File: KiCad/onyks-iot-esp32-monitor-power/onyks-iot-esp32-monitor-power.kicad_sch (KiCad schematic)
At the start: 16 parts, among them J1 Uart_con, J2 Jtag_con, SW1 reset, U1 ESP32-WROOM-32D, U2 ADS1115IDGS

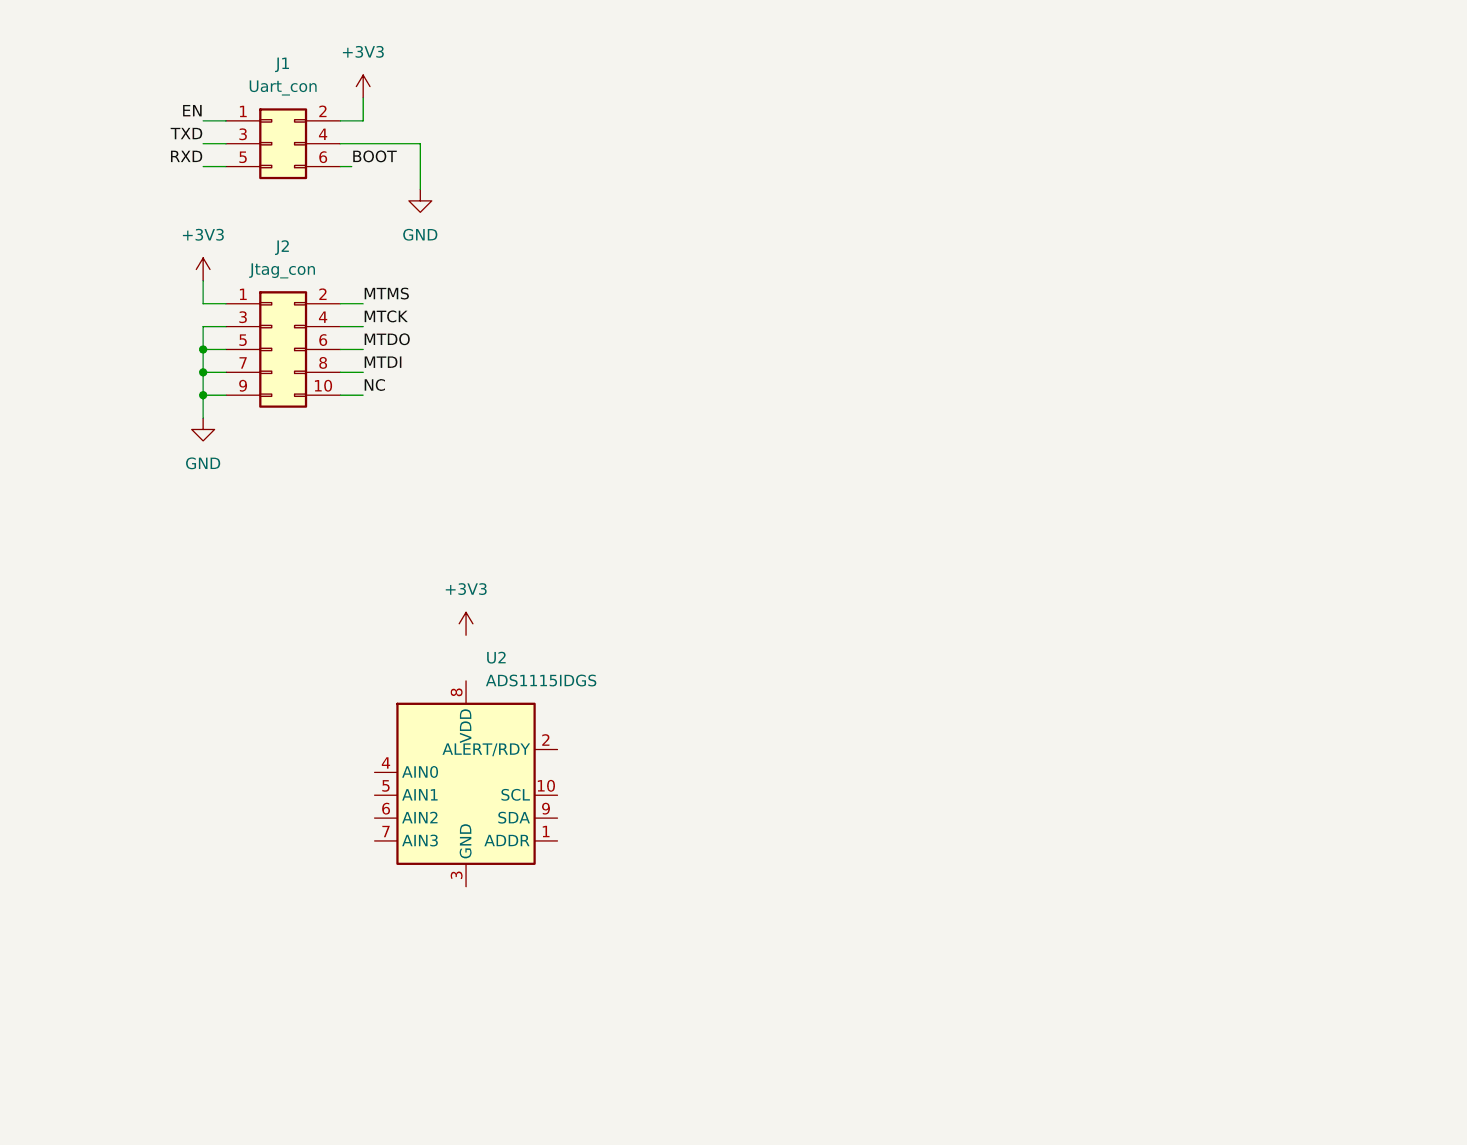
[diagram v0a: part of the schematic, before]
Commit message: Add ACS712 and ADS1115
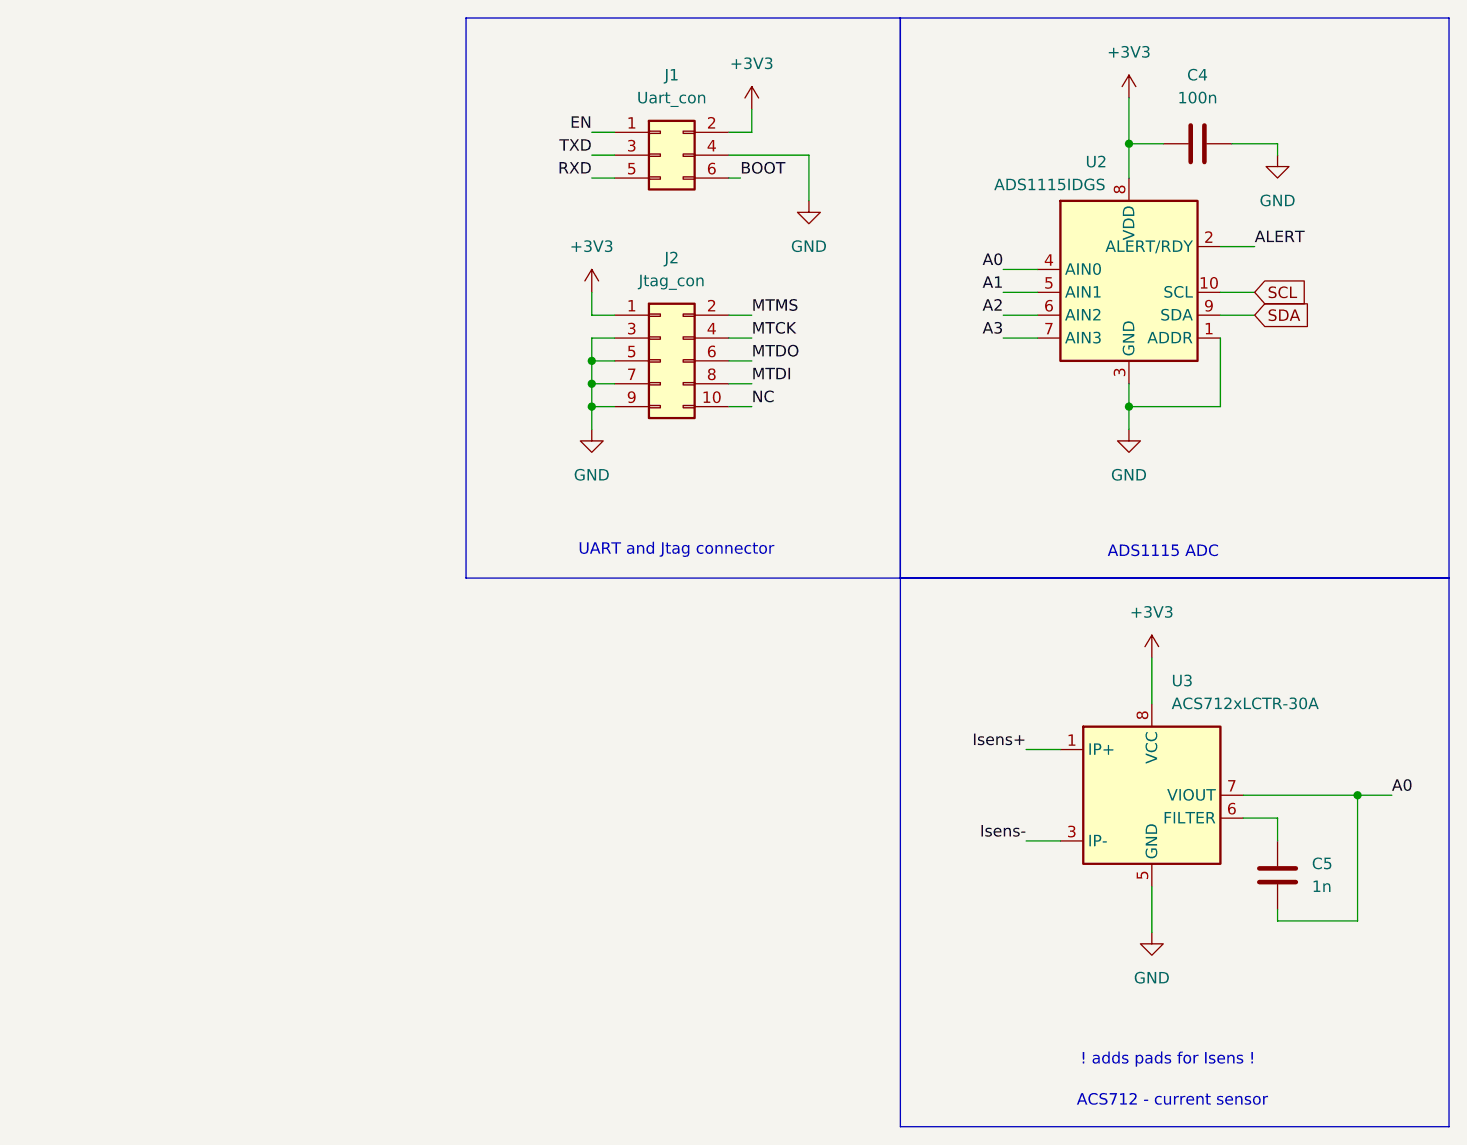
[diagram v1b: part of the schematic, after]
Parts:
- added C4: 100n, Capacitor_SMD:C_0805_2012Metric_Pad1.18x1.45mm_HandSolder, symbol Device:C
- added C5: 1n, symbol Device:C
- added U3: ACS712xLCTR-30A, Package_SO:SOIC-8_3.9x4.9mm_P1.27mm, symbol Sensor_Current:ACS712xLCTR-30A
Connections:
- net +3V3: now also U2.8 (VDD), C4.1, U3.8 (VCC)
- net ALERT: now also U2.2 (ALERT/RDY)
- net GND: now also U2.1 (ADDR), U2.3 (GND), C4.2, U3.5 (GND)
- net SCL: now also U2.10 (SCL)
- net SDA: now also U2.9 (SDA)
- net A0: now reaches U2.4 (AIN0)
- net A0: now also C5.1, U3.7 (VIOUT)
- net A1: now reaches U2.5 (AIN1)
- net A2: now reaches U2.6 (AIN2)
- net A3: now reaches U2.7 (AIN3)
- new net: C5.2, U3.6 (FILTER)
- new net Isens+: U3.1 (IP+), U3.2 (IP+)
- new net Isens-: U3.3 (IP-), U3.4 (IP-)
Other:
- note added: "! adds pads for Isens !"
- note added: "ACS712 - current sensor"
- note added: "ADS1115 ADC"
- note added: "UART and Jtag connector"
- moved on the sheet: J1, J2, U2

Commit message: edit schemat
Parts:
- added C6: 100n, symbol Device:C
- added D1: WS2812B, LED_SMD:LED_WS2812B_PLCC4_5.0x5.0mm_P3.2mm, symbol LED:WS2812B
- added J3: Conn_01x06, Connector_PinHeader_2.54mm:PinHeader_1x06_P2.54mm_Vertical, symbol Connector_Generic:Conn_01x06
- added Q1: SS8050, Package_TO_SOT_SMD:SOT-23-3, symbol Transistor_BJT:SS8050
- added Q2: SS8050, Package_TO_SOT_SMD:SOT-23, symbol Transistor_BJT:SS8050
- added R10: 1K4, symbol Device:R
- added R11, R12: 10K, symbol Device:R
- added R9: 200K, symbol Device:R
- added T1: Transformer_1P_1S, symbol Device:Transformer_1P_1S
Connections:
- net +3V3: now also C6.1, D1.1 (VDD), J3.1 (Pin_1)
- net BOOT: now also Q2.3 (C)
- net EN: now also Q1.3 (C)
- net GND: now also C6.2, D1.3 (VSS), J3.2 (Pin_2)
- net RXD: now also J3.4 (Pin_4)
- net TXD: now also J3.3 (Pin_3)
- net LED: now reaches U1.24 (IO2)
- net LED: now also D1.4 (DIN)
- new net: R10.1, T1.4 (SB)
- new net: R10.2, T1.3 (SA)
- new net: Q1.1 (B), R11.2
- new net: R9.2, T1.1 (AA)
- new net: Q2.1 (B), R12.2
- new net DTR: J3.5 (Pin_5), Q2.2 (E), R11.1
- new net RTS: J3.6 (Pin_6), Q1.2 (E), R12.1
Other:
- note added: "0~300AC 50Hz"
- note added: "UART ONYKS connector"
- note added: "WS2812B"
- moved on the sheet: C1, C2, C3, R1, R2, R3, R4, R5, R6, R7, R8, SW1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

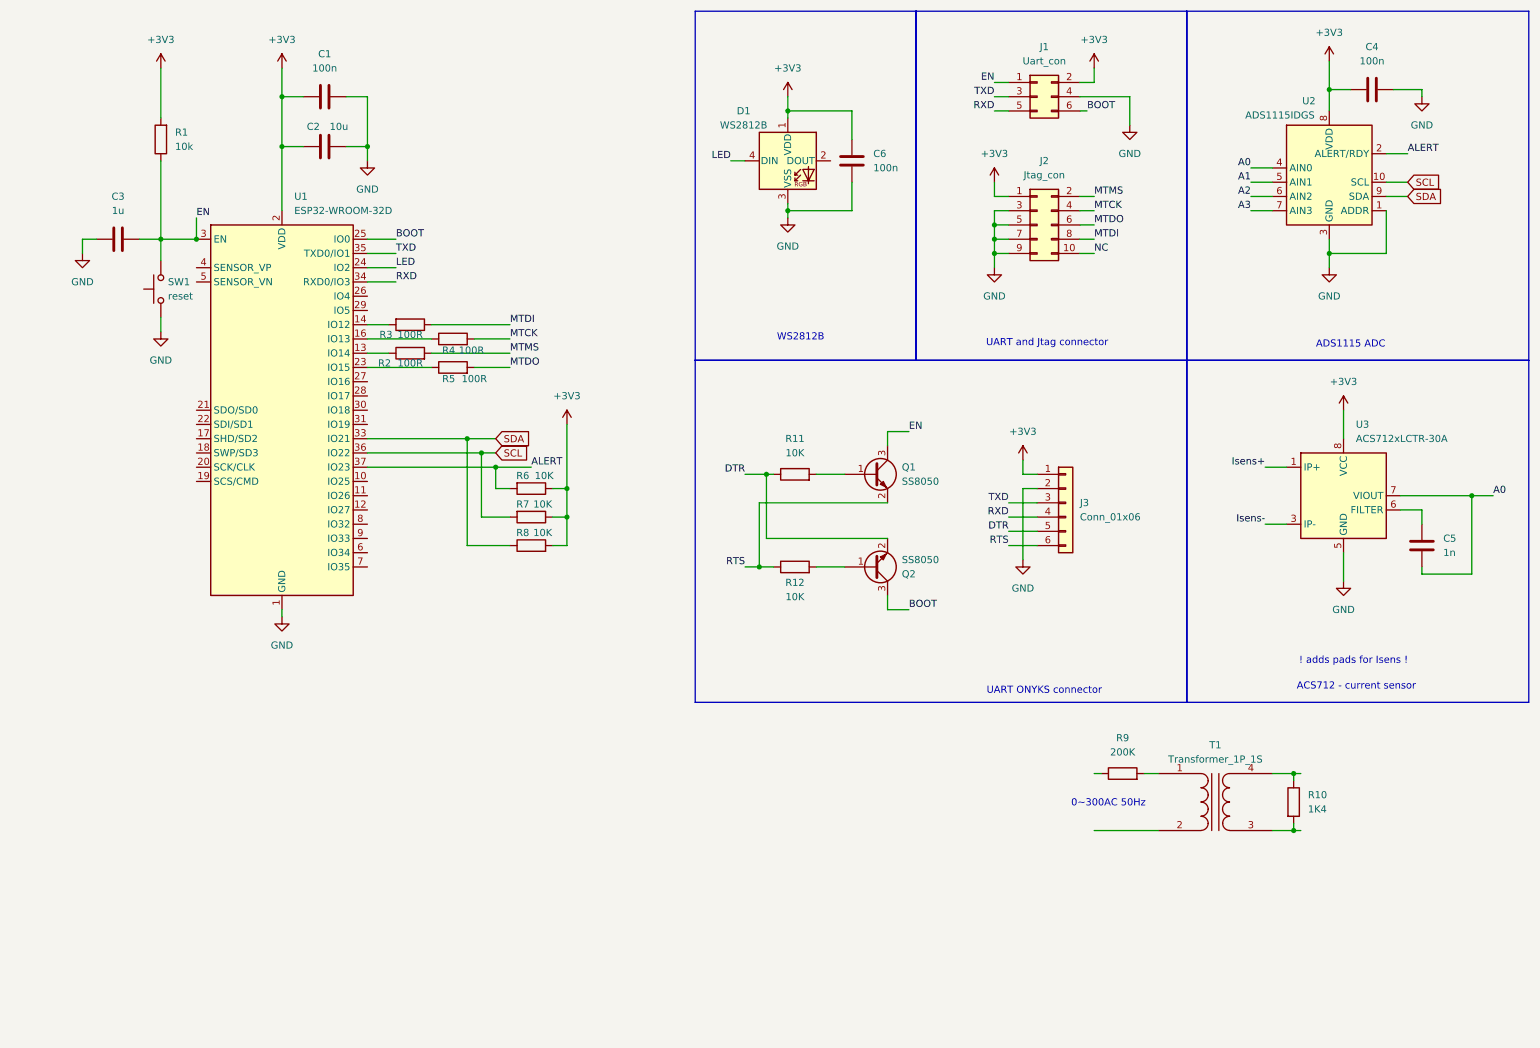
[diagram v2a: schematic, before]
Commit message: scheme v1; Add fotprints
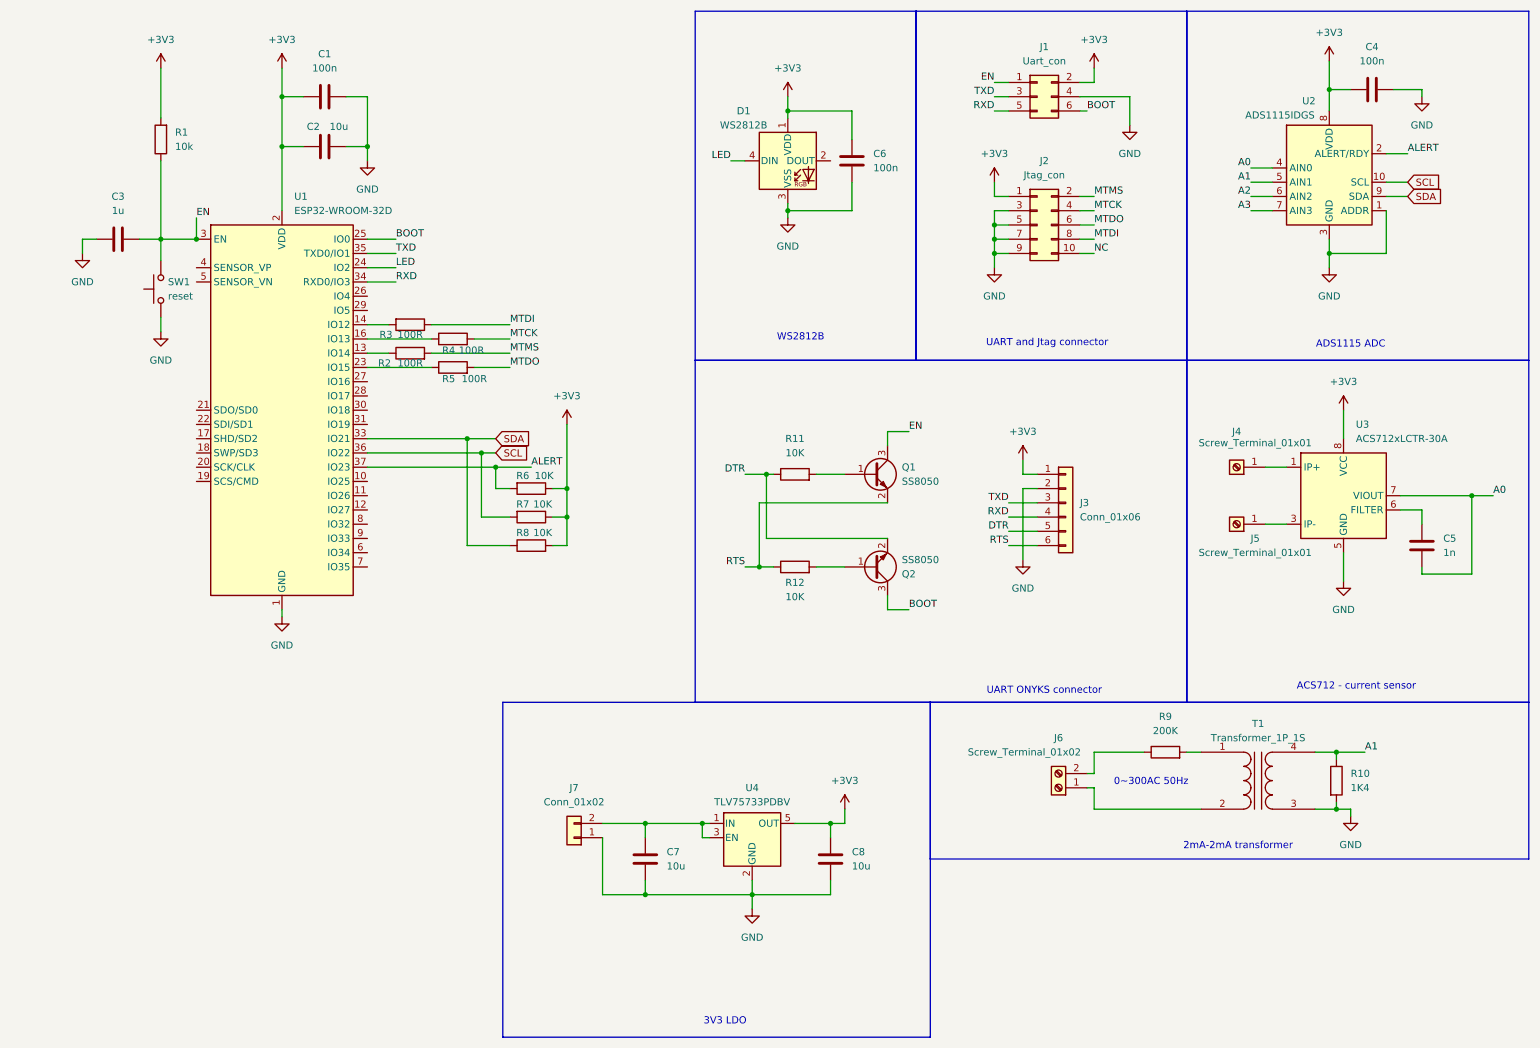
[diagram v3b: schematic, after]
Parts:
- added C7, C8: 10u, Capacitor_SMD:C_0805_2012Metric, symbol Device:C
- added J4, J5: Screw_Terminal_01x01, macmysz:Screw Terminal M4 8x8, symbol Connector:Screw_Terminal_01x01
- added J6: Screw_Terminal_01x02, TerminalBlock:TerminalBlock_bornier-2_P5.08mm, symbol Connector:Screw_Terminal_01x02
- added J7: Conn_01x02, Connector_PinHeader_2.54mm:PinHeader_1x02_P2.54mm_Vertical, symbol Connector_Generic:Conn_01x02
- added U4: TLV75733PDBV, Package_TO_SOT_SMD:SOT-23-5, symbol Regulator_Linear:TLV75733PDBV
- C1, C4: footprint Capacitor_SMD:C_0805_2012Metric_Pad1.18x1.45mm_HandSolder -> Capacitor_SMD:C_0805_2012Metric
- C2, C3, C5, C6: footprint (none) -> Capacitor_SMD:C_0805_2012Metric
- J1: footprint (none) -> Connector_IDC:IDC-Header_2x03_P2.54mm_Vertical
- J2: footprint Connector_PinSocket_1.27mm:PinSocket_2x05_P1.27mm_Vertical -> Connector_IDC:IDC-Header_2x05_P2.54mm_Vertical
- R1, R10, R11, R12, R2, R3, R4, R5, R6, R7, R8, R9: footprint (none) -> Resistor_SMD:R_0805_2012Metric
- SW1: footprint (none) -> Button_Switch_SMD:SW_Tactile_SPST_NO_Straight_CK_PTS636Sx25SMTRLFS
- T1: footprint (none) -> macmysz:ZMPT101B
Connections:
- net +3V3: now also C8.1, U4.5 (OUT)
- net A1: now also R10.1, T1.4 (SB)
- net GND: now also R10.2, T1.3 (SA), C7.2, C8.2, J7.1 (Pin_1), U4.2 (GND)
- net at T1.2 (AB): now also J6.1 (Pin_1)
- net at R9.1: now also J6.2 (Pin_2)
- net Isens+: no longer names the net of U3.1 (IP+), U3.2 (IP+)
- net Isens+: now also J4.1 (Pin_1)
- net Isens-: no longer names the net of U3.3 (IP-), U3.4 (IP-)
- net Isens-: now also J5.1 (Pin_1)
- new net: C7.1, J7.2 (Pin_2), U4.1 (IN), U4.3 (EN)
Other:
- note added: "2mA-2mA transformer"
- note added: "3V3 LDO"
- note removed: "! adds pads for Isens !"
- moved on the sheet: R10, R9, T1

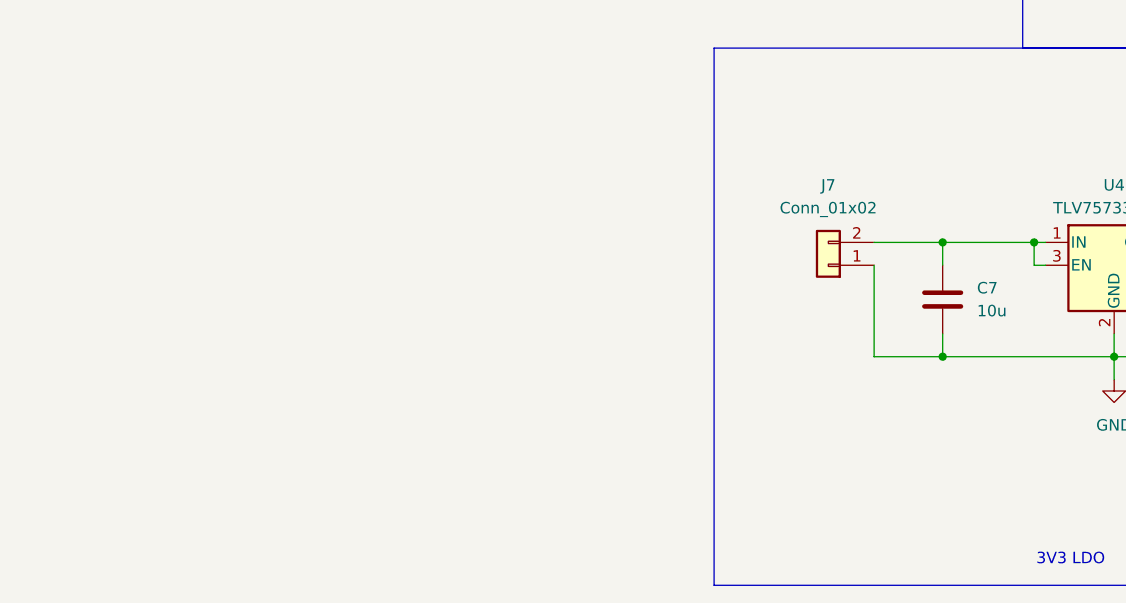
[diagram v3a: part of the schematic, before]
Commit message: Add relay to sheme (not ended)
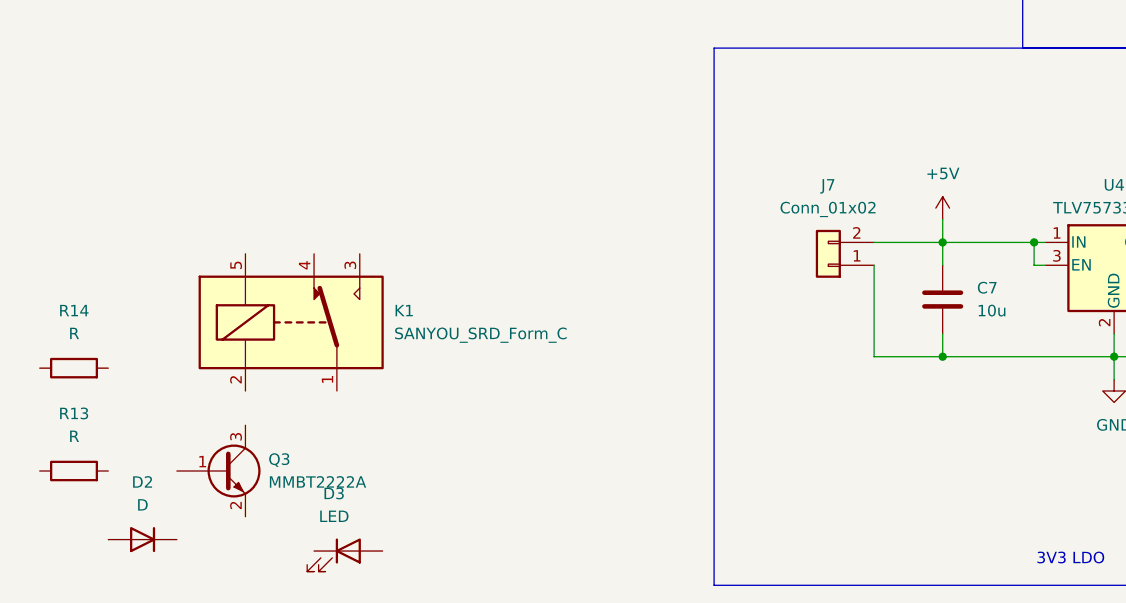
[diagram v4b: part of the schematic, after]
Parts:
- added D2: D, symbol Device:D
- added D3: LED, symbol Device:LED
- added K1: SANYOU_SRD_Form_C, Relay_THT:Relay_SPDT_SANYOU_SRD_Series_Form_C, symbol Relay:SANYOU_SRD_Form_C
- added Q3: MMBT2222A, Package_TO_SOT_SMD:SOT-23, symbol Transistor_BJT:MMBT2222A
- added R13, R14: R, symbol Device:R
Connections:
- net +5V: now reaches C7.1, J7.2 (Pin_2), U4.1 (IN), U4.3 (EN)
